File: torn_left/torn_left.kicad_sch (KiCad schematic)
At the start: 73 parts, among them J1 SJ-43514, SW1 SW_Push, SW10 SW_Push, SW11 SW_Push, SW12 SW_Push, SW13 SW_Push, SW14 SW_Push, SW15 SW_Push, SW16 SW_Push, SW17 SW_Push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

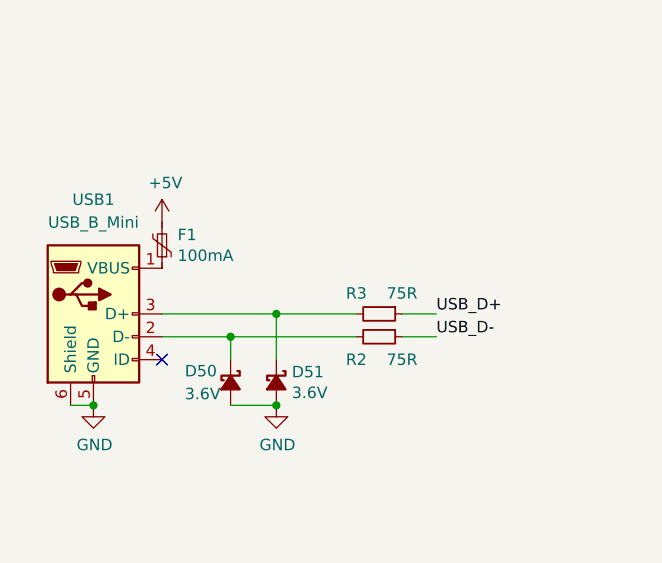
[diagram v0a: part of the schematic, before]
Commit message: changed resistor sizes to more common 1/4W 0207DIN sizes on both boards
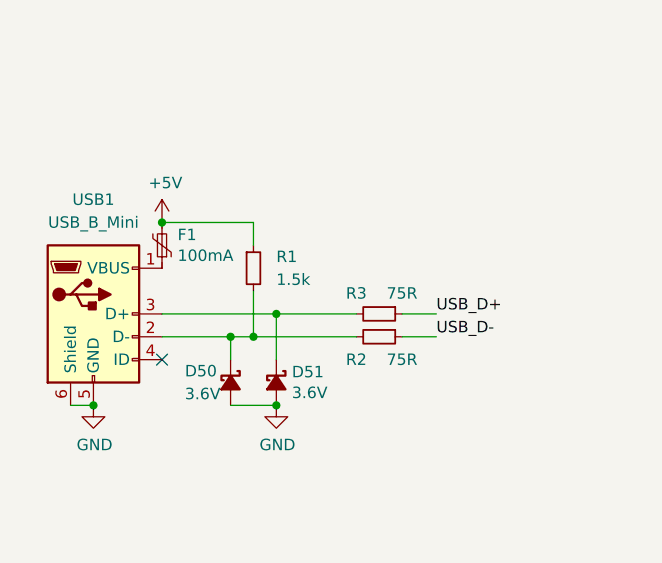
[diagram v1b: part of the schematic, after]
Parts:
- added R1: 1.5k, Resistor_THT:R_Axial_DIN0207_L6.3mm_D2.5mm_P7.62mm_Horizontal, symbol Device:R_Small
- R2, R3, R6, R7, R8: footprint footprints:R_Axial_DIN0204_L3.6mm_D1.6mm_P5.08mm_Horizontal -> Resistor_THT:R_Axial_DIN0207_L6.3mm_D2.5mm_P7.62mm_Horizontal
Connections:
- net +5V: now also R1.1
- net at D50.1 (K), R2.2, USB1.2 (D-): now also R1.2
